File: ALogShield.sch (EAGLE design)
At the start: 33 parts, among them U1 DS3231MZ/V+T

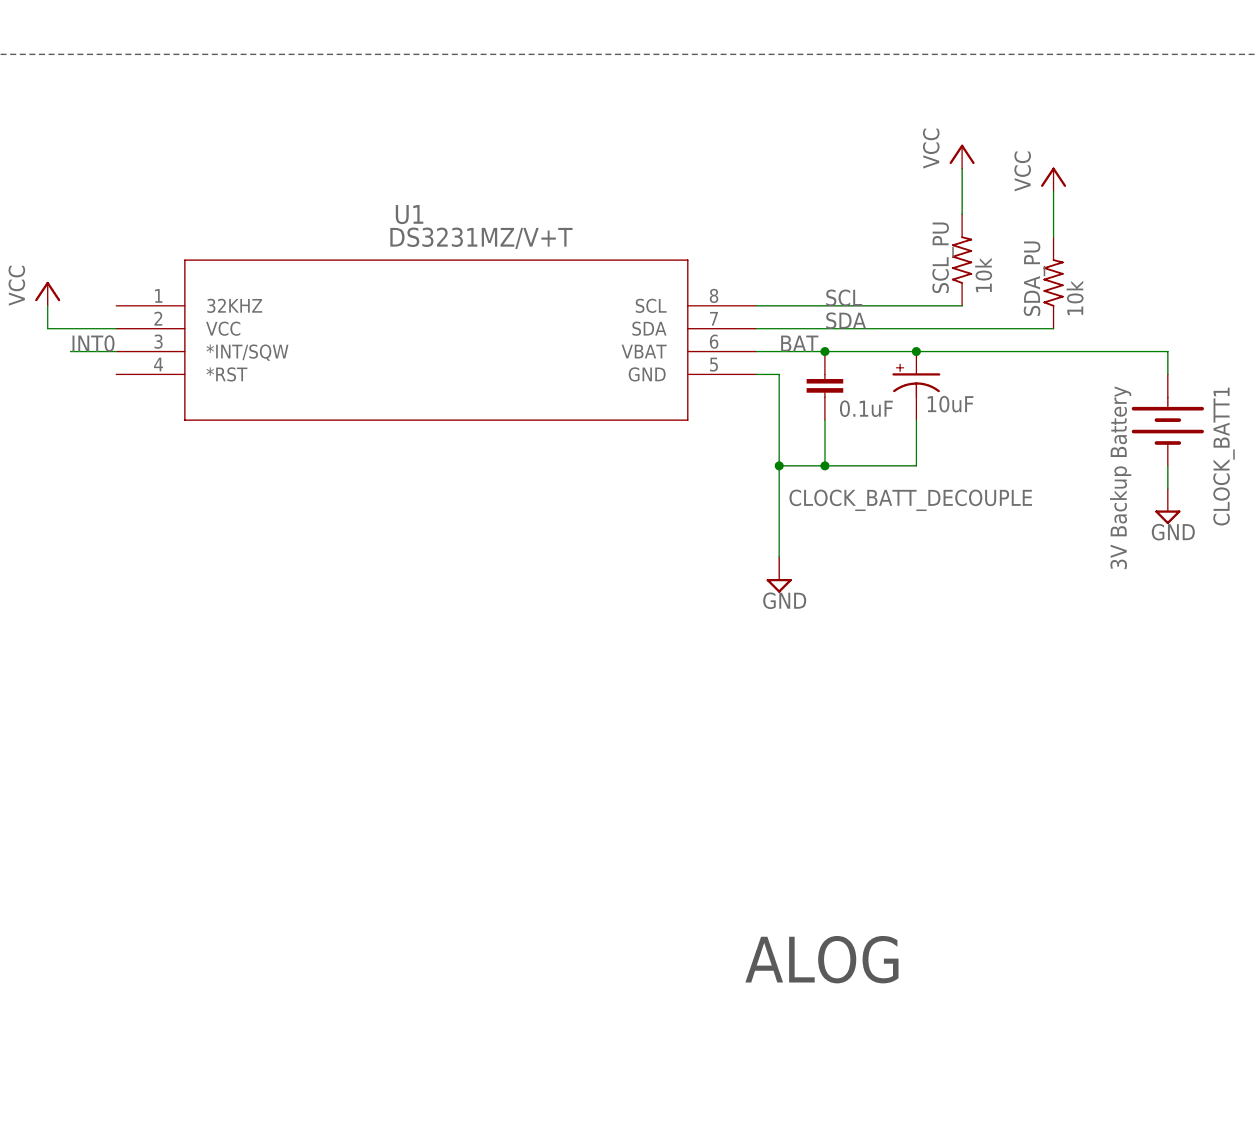
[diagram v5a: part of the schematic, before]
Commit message: Use our in-stock 3.3k-ohm pull-up resistor array, even if only 2/4 in use
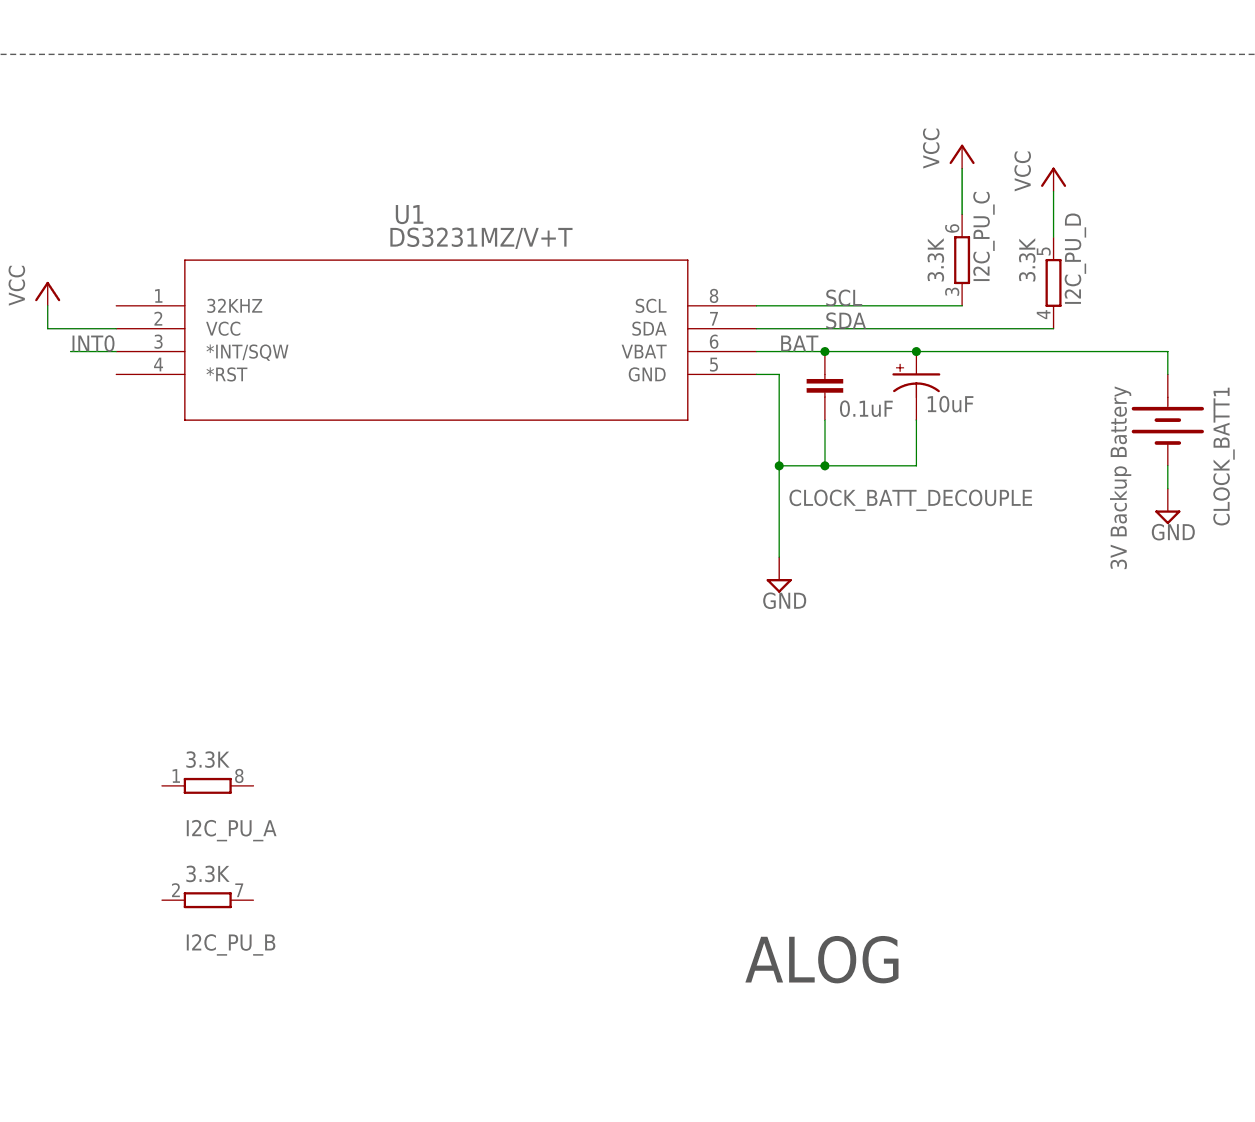
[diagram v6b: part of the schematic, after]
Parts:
- removed SCL_PU, SDA_PU: 10k, rcl:R-US_R0603
- added I2C_PU_: 3.3K, resistor-dil:4R-N0603-ARC
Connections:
- net SCL: now also I2C_PU_C.1; no longer SCL_PU.1
- net SDA: now also I2C_PU_D.1; no longer SDA_PU.1
- net VCC: now also I2C_PU_C.2, I2C_PU_D.2; no longer SCL_PU.2, SDA_PU.2
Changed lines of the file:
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@@
 <part name="SUPPLY3" library="supply2" deviceset="GND" device=""/>
 <part name="J2" library="SparkFun-Connectors" deviceset="CONN_04" device="SCREW"/>
-<part name="SCL_PU" library="rcl" deviceset="R-US_" device="R0603" value="10k"/>
-<part name="SDA_PU" library="rcl" deviceset="R-US_" device="R0603" value="10k"/>
+<part name="I2C_PU_" library="resistor-dil" deviceset="4R-N" device="0603-ARC" value="3.3K"/>
 </parts>
 <sheets>
@@
 <instance part="SUPPLY3" gate="GND" x="99.06" y="-134.62"/>
 <instance part="J2" gate="G$1" x="134.62" y="-134.62" rot="R180"/>
-<instance part="SCL_PU" gate="G$1" x="114.3" y="-398.78" rot="R90"/>
-<instance part="SDA_PU" gate="G$1" x="124.46" y="-401.32" rot="R90"/>
+<instance part="I2C_PU_" gate="A" x="30.48" y="-457.2" smashed="yes">
+<attribute name="VALUE" x="27.94" y="-455.168" size="1.778" layer="96"/>
+<attribute name="NAME" x="27.94" y="-462.788" size="1.778" layer="95"/>
+</instance>
+<instance part="I2C_PU_" gate="B" x="30.48" y="-469.9" smashed="yes">
+<attribute name="VALUE" x="27.94" y="-467.868" size="1.778" layer="96"/>
+<attribute name="NAME" x="27.94" y="-475.488" size="1.778" layer="95"/>
+</instance>
+<instance part="I2C_PU_" gate="C" x="114.3" y="-398.78" smashed="yes" rot="R90">
+<attribute name="VALUE" x="112.268" y="-401.32" size="1.778" layer="96" rot="R90"/>
+<attribute name="NAME" x="117.348" y="-401.32" size="1.778" layer="95" rot="R90"/>
+</instance>
+<instance part="I2C_PU_" gate="D" x="124.46" y="-401.32" smashed="yes" rot="R90">
+<attribute name="VALUE" x="122.428" y="-401.32" size="1.778" layer="96" rot="R90"/>
+<attribute name="NAME" x="127.508" y="-403.86" size="1.778" layer="95" rot="R90"/>
+</instance>
 </instances>
 <busses>
@@
 <wire x1="124.46" y1="-391.16" x2="124.46" y2="-396.24" width="0.1524" layer="91"/>
 <pinref part="P+5" gate="VCC" pin="VCC"/>
-<pinref part="SDA_PU" gate="G$1" pin="2"/>
+<pinref part="I2C_PU_" gate="D" pin="2"/>
 </segment>
 <segment>
 <wire x1="114.3" y1="-388.62" x2="114.3" y2="-393.7" width="0.1524" layer="91"/>
 <pinref part="P+7" gate="VCC" pin="VCC"/>
-<pinref part="SCL_PU" gate="G$1" pin="2"/>
+<pinref part="I2C_PU_" gate="C" pin="2"/>
 </segment>
 <segment>
@@
 <label x="99.06" y="-403.86" size="1.778" layer="95"/>
 <pinref part="U1" gate="A" pin="SCL"/>
-<pinref part="SCL_PU" gate="G$1" pin="1"/>
+<pinref part="I2C_PU_" gate="C" pin="1"/>
 </segment>
 </net>
@@
 <label x="99.06" y="-406.4" size="1.778" layer="95"/>
 <pinref part="U1" gate="A" pin="SDA"/>
-<pinref part="SDA_PU" gate="G$1" pin="1"/>
-</segment>
-</net>
+<pinref part="I2C_PU_" gate="D" pin="1"/>
+</segment>
+</net>

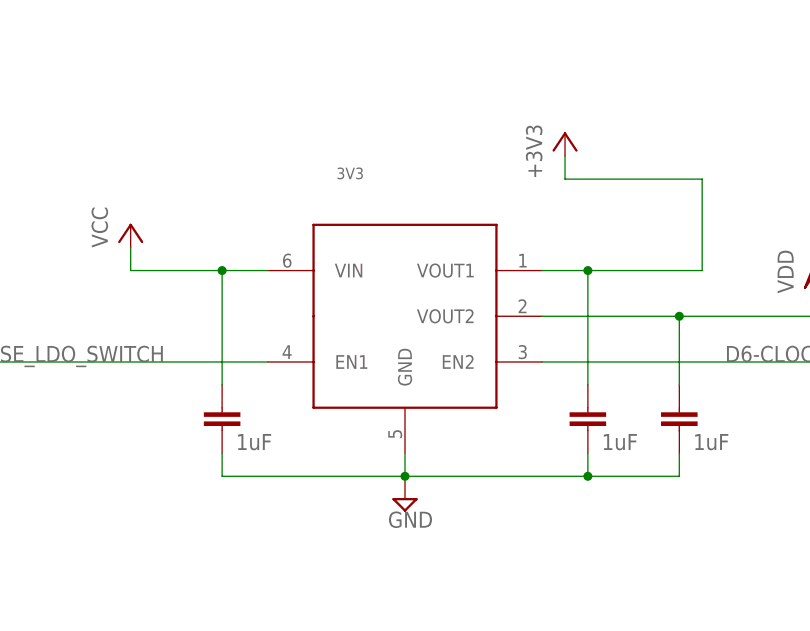
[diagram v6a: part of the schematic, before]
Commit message: 3V3 with wide pads
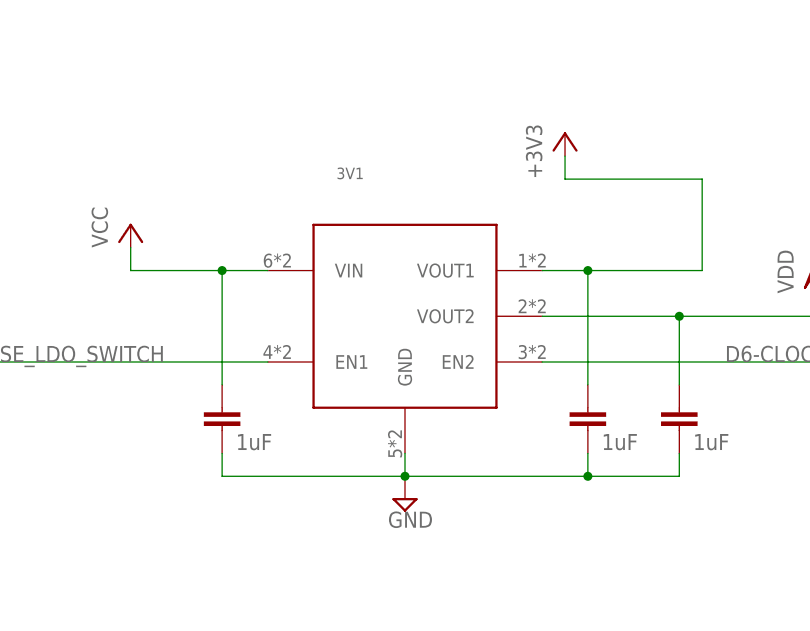
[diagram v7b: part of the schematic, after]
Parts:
- removed 3V3: (no value), csandell:MIC5380
- added 3V1: MIC5380_LARGE_PADS, csandell:MIC5380_LARGE_PADS
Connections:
- net +3V3: now also 3V1.VOUT1; no longer 3V3.VOUT1
- net D4-SENSE_LDO_SWITCH: now also 3V1.EN1; no longer 3V3.EN1
- net D6-CLOCK_SD_SWITCH: now also 3V1.EN2; no longer 3V3.EN2
- net GND: now also 3V1.GND; no longer 3V3.GND
- net VCC: now also 3V1.VIN; no longer 3V3.VIN
- net VDD: now also 3V1.VOUT2; no longer 3V3.VOUT2
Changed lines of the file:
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@@
 <part name="SD_3V6" library="supply1" deviceset="VDD" device=""/>
 <part name="+3V16" library="supply1" deviceset="+3V3" device=""/>
-<part name="3V3" library="csandell" deviceset="MIC5380" device=""/>
 <part name="+3V4" library="supply1" deviceset="+3V3" device=""/>
 <part name="H2" library="SparkFun" deviceset="M08" device="3.5MM-8"/>
@@
 <part name="J2" library="SparkFun-Connectors" deviceset="CONN_04" device="SCREW"/>
 <part name="I2C_PU_" library="resistor-dil" deviceset="4R-N" device="0603-ARC" value="3.3K"/>
+<part name="3V1" library="csandell" deviceset="MIC5380_LARGE_PADS" device=""/>
 </parts>
 <sheets>
@@
 <instance part="SD_3V6" gate="G$1" x="307.34" y="-276.86"/>
 <instance part="+3V16" gate="G$1" x="20.32" y="-129.54"/>
-<instance part="3V3" gate="G$1" x="261.62" y="-38.1"/>
 <instance part="+3V4" gate="G$1" x="27.94" y="-124.46"/>
 <instance part="H2" gate="G$1" x="55.88" y="-121.92" rot="R180"/>
@@
 <attribute name="NAME" x="127.508" y="-403.86" size="1.778" layer="95" rot="R90"/>
 </instance>
+<instance part="3V1" gate="G$1" x="261.62" y="-38.1"/>
 </instances>
 <busses>
@@
 <pinref part="P+22" gate="VCC" pin="VCC"/>
 <wire x1="231.14" y1="-33.02" x2="231.14" y2="-30.48" width="0.1524" layer="91"/>
-<pinref part="3V3" gate="G$1" pin="VIN"/>
+<pinref part="3V1" gate="G$1" pin="VIN"/>
 </segment>
 <segment>
@@
 <wire x1="241.3" y1="-53.34" x2="241.3" y2="-55.88" width="0.1524" layer="91"/>
 <junction x="281.94" y="-55.88"/>
-<pinref part="3V3" gate="G$1" pin="GND"/>
+<pinref part="3V1" gate="G$1" pin="GND"/>
 </segment>
 <segment>
@@
 <wire x1="294.64" y1="-33.02" x2="294.64" y2="-22.86" width="0.1524" layer="91"/>
 <wire x1="294.64" y1="-22.86" x2="279.4" y2="-22.86" width="0.1524" layer="91"/>
-<pinref part="3V3" gate="G$1" pin="VOUT1"/>
+<pinref part="3V1" gate="G$1" pin="VOUT1"/>
 </segment>
 <segment>
@@
 <pinref part="SD_3V4" gate="G$1" pin="VDD"/>
 <wire x1="307.34" y1="-38.1" x2="307.34" y2="-35.56" width="0.1524" layer="91"/>
-<pinref part="3V3" gate="G$1" pin="VOUT2"/>
 <junction x="292.1" y="-38.1"/>
+<pinref part="3V1" gate="G$1" pin="VOUT2"/>
 </segment>
 <segment>
@@
 <wire x1="246.38" y1="-43.18" x2="208.28" y2="-43.18" width="0.1524" layer="91"/>
 <label x="208.28" y="-43.18" size="1.778" layer="95"/>
-<pinref part="3V3" gate="G$1" pin="EN1"/>
+<pinref part="3V1" gate="G$1" pin="EN1"/>
 </segment>
 <segment>
@@
 <wire x1="276.86" y1="-43.18" x2="325.12" y2="-43.18" width="0.1524" layer="91"/>
 <label x="297.18" y="-43.18" size="1.778" layer="95"/>
-<pinref part="3V3" gate="G$1" pin="EN2"/>
-</segment>
-<segment>
+<pinref part="3V1" gate="G$1" pin="EN2"/>
+</segment>
+<segment>

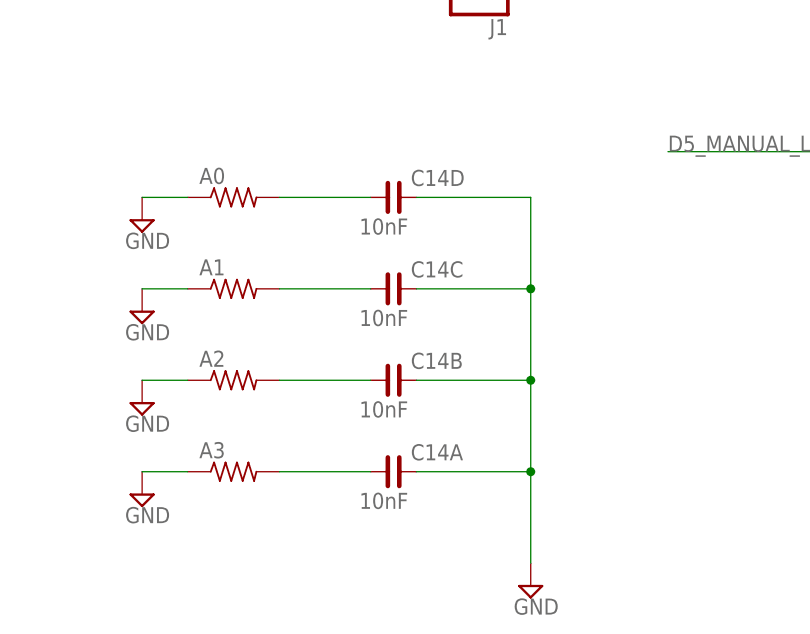
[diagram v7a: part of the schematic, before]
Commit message: Long pads on cap array: easier soldering, we hope
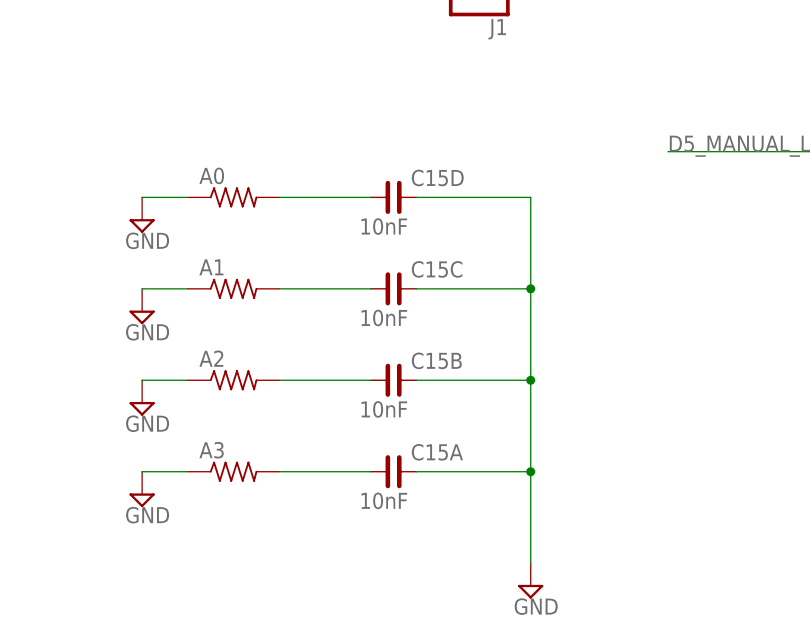
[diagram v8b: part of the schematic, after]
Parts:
- removed C14: 10nF, rc-master-smd:CCA_ECJ-1206
- added C15: 10nF, rc-master-smd:CCA_
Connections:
- new net N$1: A0.2, C15D.1
- new net N$2: A1.2, C15C.1
- new net N$3: A2.2, C15B.1
- new net N$4: A3.2, C15A.1
- net A0: no longer A0.2, C14D.1
- net A1: no longer A1.2, C14C.1
- net A2: no longer A2.2, C14B.1
- net A3: no longer A3.2, C14A.1
- net GND: now also C15A.2, C15B.2, C15C.2, C15D.2; no longer C14A.2, C14B.2, C14C.2, C14D.2
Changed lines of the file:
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@@
 <part name="SUPPLY52" library="supply2" deviceset="GND" device=""/>
 <part name="RESET" library="SparkFun-Electromechanical" deviceset="SWITCH-MOMENTARY-2" device="PTH" value="Reset"/>
-<part name="C14" library="rc-master-smd" deviceset="CCA_" device="ECJ-1206" value="10nF"/>
 <part name="SUPPLY53" library="supply2" deviceset="GND" device=""/>
 <part name="CLOCK_BATT_DECOUP" library="rcl" deviceset="C-EU" device="C0603" value="0.1uF"/>
@@
 <part name="I2C_PU_" library="resistor-dil" deviceset="4R-N" device="0603-ARC" value="3.3K"/>
 <part name="3V1" library="csandell" deviceset="MIC5380_LARGE_PADS" device=""/>
+<part name="C15" library="rc-master-smd" deviceset="CCA_" device="" value="10nF"/>
 </parts>
 <sheets>
@@
 <instance part="SUPPLY52" gate="GND" x="109.22" y="-200.66"/>
 <instance part="RESET" gate="G$1" x="157.48" y="-182.88" rot="R90"/>
-<instance part="C14" gate="A" x="48.26" y="-195.58"/>
-<instance part="C14" gate="B" x="48.26" y="-185.42"/>
-<instance part="C14" gate="C" x="48.26" y="-175.26"/>
-<instance part="C14" gate="D" x="48.26" y="-165.1"/>
 <instance part="SUPPLY53" gate="GND" x="63.5" y="-208.28"/>
 <instance part="CLOCK_BATT_DECOUP" gate="G$1" x="99.06" y="-411.48" smashed="yes">
@@
 </instance>
 <instance part="3V1" gate="G$1" x="261.62" y="-38.1"/>
+<instance part="C15" gate="A" x="48.26" y="-195.58"/>
+<instance part="C15" gate="B" x="48.26" y="-185.42"/>
+<instance part="C15" gate="C" x="48.26" y="-175.26"/>
+<instance part="C15" gate="D" x="48.26" y="-165.1"/>
 </instances>
 <busses>
@@
 <pinref part="SUPPLY53" gate="GND" pin="GND"/>
 <wire x1="63.5" y1="-165.1" x2="63.5" y2="-175.26" width="0.1524" layer="91"/>
-<pinref part="C14" gate="D" pin="2"/>
+<pinref part="C15" gate="D" pin="2"/>
 <wire x1="63.5" y1="-175.26" x2="63.5" y2="-185.42" width="0.1524" layer="91"/>
 <wire x1="63.5" y1="-185.42" x2="63.5" y2="-195.58" width="0.1524" layer="91"/>
 <wire x1="63.5" y1="-195.58" x2="63.5" y2="-205.74" width="0.1524" layer="91"/>
-<wire x1="50.8" y1="-165.1" x2="63.5" y2="-165.1" width="0.1524" layer="91"/>
-<pinref part="C14" gate="C" pin="2"/>
+<wire x1="63.5" y1="-165.1" x2="50.8" y2="-165.1" width="0.1524" layer="91"/>
+<pinref part="C15" gate="C" pin="2"/>
 <wire x1="50.8" y1="-175.26" x2="63.5" y2="-175.26" width="0.1524" layer="91"/>
 <junction x="63.5" y="-175.26"/>
-<pinref part="C14" gate="B" pin="2"/>
+<pinref part="C15" gate="B" pin="2"/>
 <wire x1="50.8" y1="-185.42" x2="63.5" y2="-185.42" width="0.1524" layer="91"/>
 <junction x="63.5" y="-185.42"/>
-<pinref part="C14" gate="A" pin="2"/>
+<pinref part="C15" gate="A" pin="2"/>
 <wire x1="50.8" y1="-195.58" x2="63.5" y2="-195.58" width="0.1524" layer="91"/>
 <junction x="63.5" y="-195.58"/>
@@
 <pinref part="H2" gate="G$1" pin="5"/>
 </segment>
-<segment>
-<pinref part="C14" gate="B" pin="1"/>
-<pinref part="A2" gate="G$1" pin="2"/>
-<wire x1="45.72" y1="-185.42" x2="35.56" y2="-185.42" width="0.1524" layer="91"/>
-</segment>
 </net>
 <net name="D3-INT1" class="0">
@@
 <pinref part="H2" gate="G$1" pin="1"/>
 </segment>
-<segment>
-<pinref part="A0" gate="G$1" pin="2"/>
-<pinref part="C14" gate="D" pin="1"/>
-<wire x1="35.56" y1="-165.1" x2="45.72" y2="-165.1" width="0.1524" layer="91"/>
-</segment>
 </net>
 <net name="A3" class="0">
@@
 <label x="45.72" y="-129.54" size="1.778" layer="95"/>
 <pinref part="H2" gate="G$1" pin="7"/>
-</segment>
-<segment>
-<pinref part="A3" gate="G$1" pin="2"/>
-<pinref part="C14" gate="A" pin="1"/>
-<wire x1="35.56" y1="-195.58" x2="45.72" y2="-195.58" width="0.1524" layer="91"/>
 </segment>
 </net>
@@
 <pinref part="H2" gate="G$1" pin="3"/>
 </segment>
-<segment>
-<pinref part="A1" gate="G$1" pin="2"/>
-<pinref part="C14" gate="C" pin="1"/>
-<wire x1="35.56" y1="-175.26" x2="45.72" y2="-175.26" width="0.1524" layer="91"/>
-</segment>
 </net>
 <net name="CS-SD" class="0">
@@
 </segment>
 </net>
+<net name="N$1" class="0">
+<segment>
+<pinref part="A0" gate="G$1" pin="2"/>
+<pinref part="C15" gate="D" pin="1"/>
+<wire x1="35.56" y1="-165.1" x2="45.72" y2="-165.1" width="0.1524" layer="91"/>
+</segment>
+</net>
+<net name="N$2" class="0">
+<segment>
+<pinref part="A1" gate="G$1" pin="2"/>
+<pinref part="C15" gate="C" pin="1"/>
+<wire x1="35.56" y1="-175.26" x2="45.72" y2="-175.26" width="0.1524" layer="91"/>
+</segment>
+</net>
+<net name="N$3" class="0">
+<segment>
+<pinref part="A2" gate="G$1" pin="2"/>
+<pinref part="C15" gate="B" pin="1"/>
+<wire x1="35.56" y1="-185.42" x2="45.72" y2="-185.42" width="0.1524" layer="91"/>
+</segment>
+</net>
+<net name="N$4" class="0">
+<segment>
+<pinref part="C15" gate="A" pin="1"/>
+<pinref part="A3" gate="G$1" pin="2"/>
+<wire x1="45.72" y1="-195.58" x2="35.56" y2="-195.58" width="0.1524" layer="91"/>
+</segment>
+</net>
